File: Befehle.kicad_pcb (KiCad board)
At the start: 2 copper layers, 100 x 160 mm, 79 parts, among them J1 Conn_02x10_Odd_Even, J2 Conn_01x02, J3 Conn_01x04, J4 Conn_02x10_Odd_Even, J5 Conn_01x02, J6 Conn_01x03, U1 74LS14, U2 74LS541, U3 74LS540, U4 74LS139, U5 74LS373, U6 74540, U7 7402, U8 7408, U9 7400

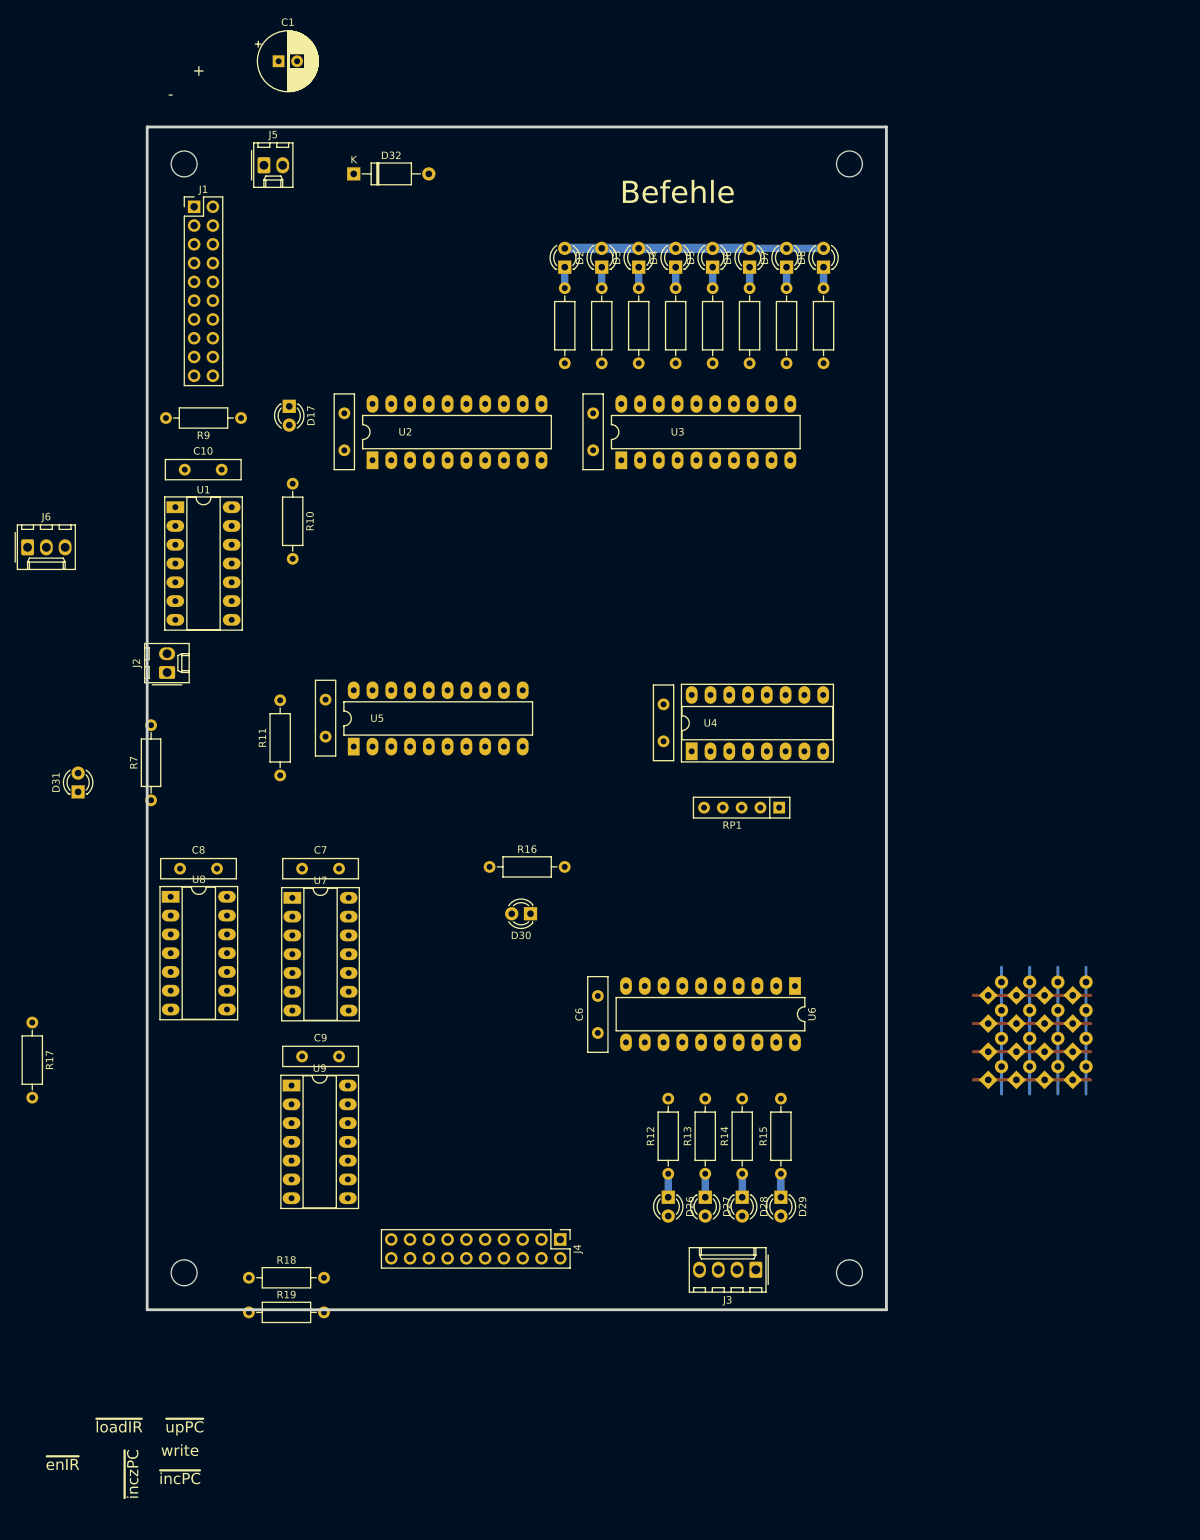
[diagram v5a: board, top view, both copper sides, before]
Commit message: Befehle: An der Platine weitergearbeitet
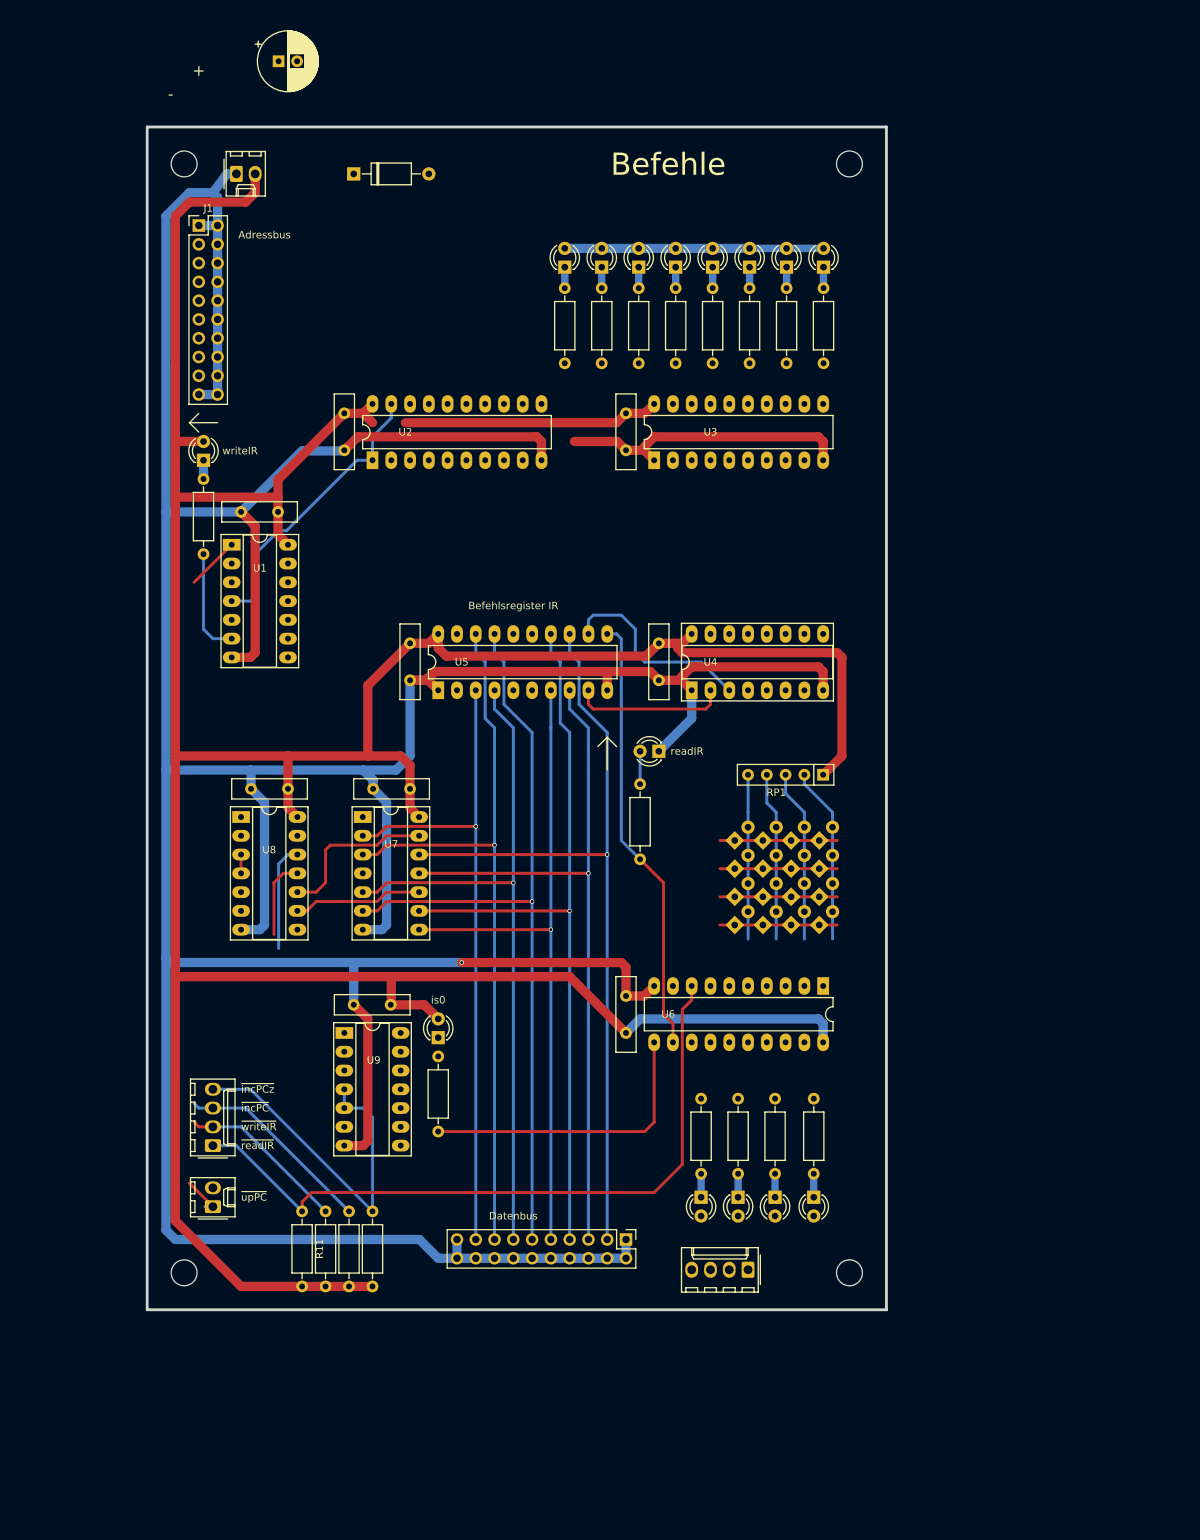
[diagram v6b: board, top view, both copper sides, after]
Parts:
- removed the R7 at (19.0, 111.1)
- J6: value Conn_01x03 -> Conn_01x04; footprint Connector_Molex:Molex_KK-254_AE-6410-03A_1x03_P2.54mm_Vertical -> Connector_Molex:Molex_KK-254_AE-6410-04A_1x04_P2.54mm_Vertical
- moved R9 118.0 mm to (42.6, 176.9), turned to 90 degrees
- moved J6 84.7 mm to (27.4, 157.8), turned to 90 degrees
- moved J2 72.5 mm to (27.4, 166.1)
- moved R11 59.0 mm to (39.5, 166.7), turned to 270 degrees
- moved D31 59.0 mm to (57.9, 143.2)
- moved R17 55.1 mm to (57.9, 145.8)
- moved D16 40.2 mm to (109.4, 120.4)
- moved D21 40.2 mm to (109.4, 124.2)
- moved D25 40.2 mm to (109.4, 128.0)
- moved D12 40.2 mm to (109.4, 116.6)
- moved D13 40.2 mm to (98.0, 120.4)
- moved D14 40.2 mm to (101.8, 120.4)
- moved D15 40.2 mm to (105.6, 120.4)
- moved D18 40.2 mm to (98.0, 124.2)
- moved D19 40.2 mm to (101.8, 124.2)
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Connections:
- J2 pad 1: loadIR -> ~upPC
- J2 pad 2: enableR -> Net-(J2-Pad2)
- J6 pad 1: upPC -> ~readIR
- J6 pad 2: incPCz -> ~writeIR
- J6 pad 3: incPC -> ~incPC
- R11 pad 1: loadIR -> ~readIR
- R9 pad 2: enableR -> ~writeIR
- U1 pad 1: enableR -> ~writeIR
- U5 pad 12: /a4 -> /b1
- U5 pad 13: /DB4 -> /DB7
- U5 pad 16: /b0 -> /a3
- U5 pad 17: /DB6 -> /DB3
- U5 pad 18: /DB7 -> /DB1
- U5 pad 19: /b1 -> /a1
- U5 pad 4: /DB1 -> /DB2
- U5 pad 5: /a1 -> /a2
- U5 pad 6: /a2 -> /a4
- U5 pad 7: /DB2 -> /DB4
- U5 pad 8: /DB3 -> /DB6
- U5 pad 9: /a3 -> /b0
- U6 pad 8: loadIR -> ~readIR
- U8 pad 14: Vcc -> VCC
- U8 pad 7: Gnd -> GND
- U9 pad 2: incPCz -> /incPCz
- U9 pad 6: incPCz -> /incPCz
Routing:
- net GND: track 0.00 -> 645.2 mm, vias 0 -> 1
- net VCC: track 35.1 -> 550.7 mm
- net /DB7: track 0.00 -> 109.5 mm, vias 0 -> 1
- net /DB3: track 0.00 -> 107.5 mm, vias 0 -> 1
- net /DB5: track 0.00 -> 103.3 mm, vias 0 -> 1
- net /DB1: track 0.00 -> 101.3 mm, vias 0 -> 1
- net /DB6: track 0.00 -> 98.3 mm, vias 0 -> 1
- net /DB2: track 0.00 -> 96.2 mm, vias 0 -> 1
- net ~readIR: track 0.00 -> 95.2 mm
- net /DB4: track 0.00 -> 92.1 mm, vias 0 -> 1
- net /DB0: track 0.00 -> 90.1 mm, vias 0 -> 1
- net Net-(R16-Pad2): track 0.00 -> 59.7 mm
- net ~incPCz: track 0.00 -> 48.0 mm
- net ~incPC: track 0.00 -> 41.5 mm
- net Net-(R17-Pad2): track 0.00 -> 40.5 mm
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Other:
- board text added: "Adressbus"
- board text added: "Befehlsregister IR"
- board text added: "Datenbus"
- board text added: "is0"
- board text added: "readIR"
- board text added: "writeIR"
- board text added: "~incPCz"
- board text added: "~readIR"
- board text added: "~writeIR"
- board text removed: "write"
- board text removed: "~enIR"
- board text removed: "~inczPC"
- board text removed: "~loadIR"

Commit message: Befehle: Platine fertig (TODO: Kontrolle)
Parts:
- U2, U3, U5, U6: footprint Package_DIP:DIP-20_W7.62mm_LongPads -> Package_DIP:DIP-20_W7.62mm_Socket_LongPads
- moved C1 16.1 mm to (41.4, 26.4), turned to 270 degrees
- moved C2 7.75 mm to (51.5, 63.2)
- moved U2 7.75 mm to (55.3, 69.6)
- moved R8 5.03 mm to (115.0, 51.8)
- moved D8 5.03 mm to (115.0, 39.1)
- moved R7 4.95 mm to (110.0, 51.8)
- moved D7 4.95 mm to (110.0, 39.1)
- moved R6 4.87 mm to (104.9, 51.8)
- moved D6 4.87 mm to (104.9, 39.1)
- moved R5 4.79 mm to (99.8, 51.8)
- moved D5 4.79 mm to (99.8, 39.1)
- moved R4 4.71 mm to (94.7, 51.8)
- moved D4 4.71 mm to (94.7, 39.1)
- moved R3 4.63 mm to (89.6, 51.8)
- moved D3 4.63 mm to (89.6, 39.1)
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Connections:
- U3 pad 2: /a7 -> /b1
- U3 pad 3: /a6 -> /b0
- U4 pad 10: (no net) -> Net-(U4-Pad10)
- U4 pad 11: (no net) -> Net-(U4-Pad11)
- U4 pad 12: (no net) -> Net-(U4-Pad12)
- U4 pad 13: (no net) -> VCC
- U4 pad 14: (no net) -> VCC
- U4 pad 15: (no net) -> VCC
- U4 pad 9: (no net) -> Net-(U4-Pad9)
- U6 pad 13: (no net) -> Net-(U6-Pad13)
- U6 pad 14: (no net) -> Net-(U6-Pad14)
- U6 pad 6: (no net) -> VCC
- U6 pad 7: (no net) -> VCC
- U9 pad 10: (no net) -> VCC
- U9 pad 11: (no net) -> Net-(U9-Pad11)
- U9 pad 12: (no net) -> VCC
- U9 pad 13: (no net) -> VCC
- U9 pad 14: Vcc -> VCC
- U9 pad 8: (no net) -> Net-(U9-Pad8)
- U9 pad 9: (no net) -> VCC
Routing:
- net VCC: track 550.7 -> 723.1 mm
- net /is0: track 0.00 -> 127.4 mm, vias 0 -> 1
- net /a0: track 0.00 -> 84.1 mm, vias 0 -> 1
- net ~writeIR: track 30.0 -> 110.6 mm
- net GND: track 645.2 -> 722.2 mm, vias 1 -> 3
- net /a2: track 0.00 -> 73.9 mm, vias 0 -> 1
- net /a1: track 0.00 -> 69.8 mm, vias 0 -> 1
- net /AB7: track 0.00 -> 68.0 mm
- net /AB6: track 0.00 -> 64.0 mm
- net /v0: track 23.8 -> 87.0 mm
- net /a4: track 0.00 -> 61.7 mm, vias 0 -> 1
- net /a3: track 0.00 -> 59.7 mm, vias 0 -> 1
- net /AB5: track 0.00 -> 59.7 mm
- net /v1: track 23.3 -> 80.5 mm
- net /AB4: track 0.00 -> 55.7 mm
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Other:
- board text added: "0"
- board text added: "1"
- board text added: "2"
- board text added: "3"
- board text added: "4"
- board text added: "5"
- board text added: "Adresse"
- board text added: "Befehl"
- board text added: "Befehlsdecoder"
- board text added: "Datenbus ist 0"
- board text added: "Mikroprogrammadresse"
- board text removed: "is0"

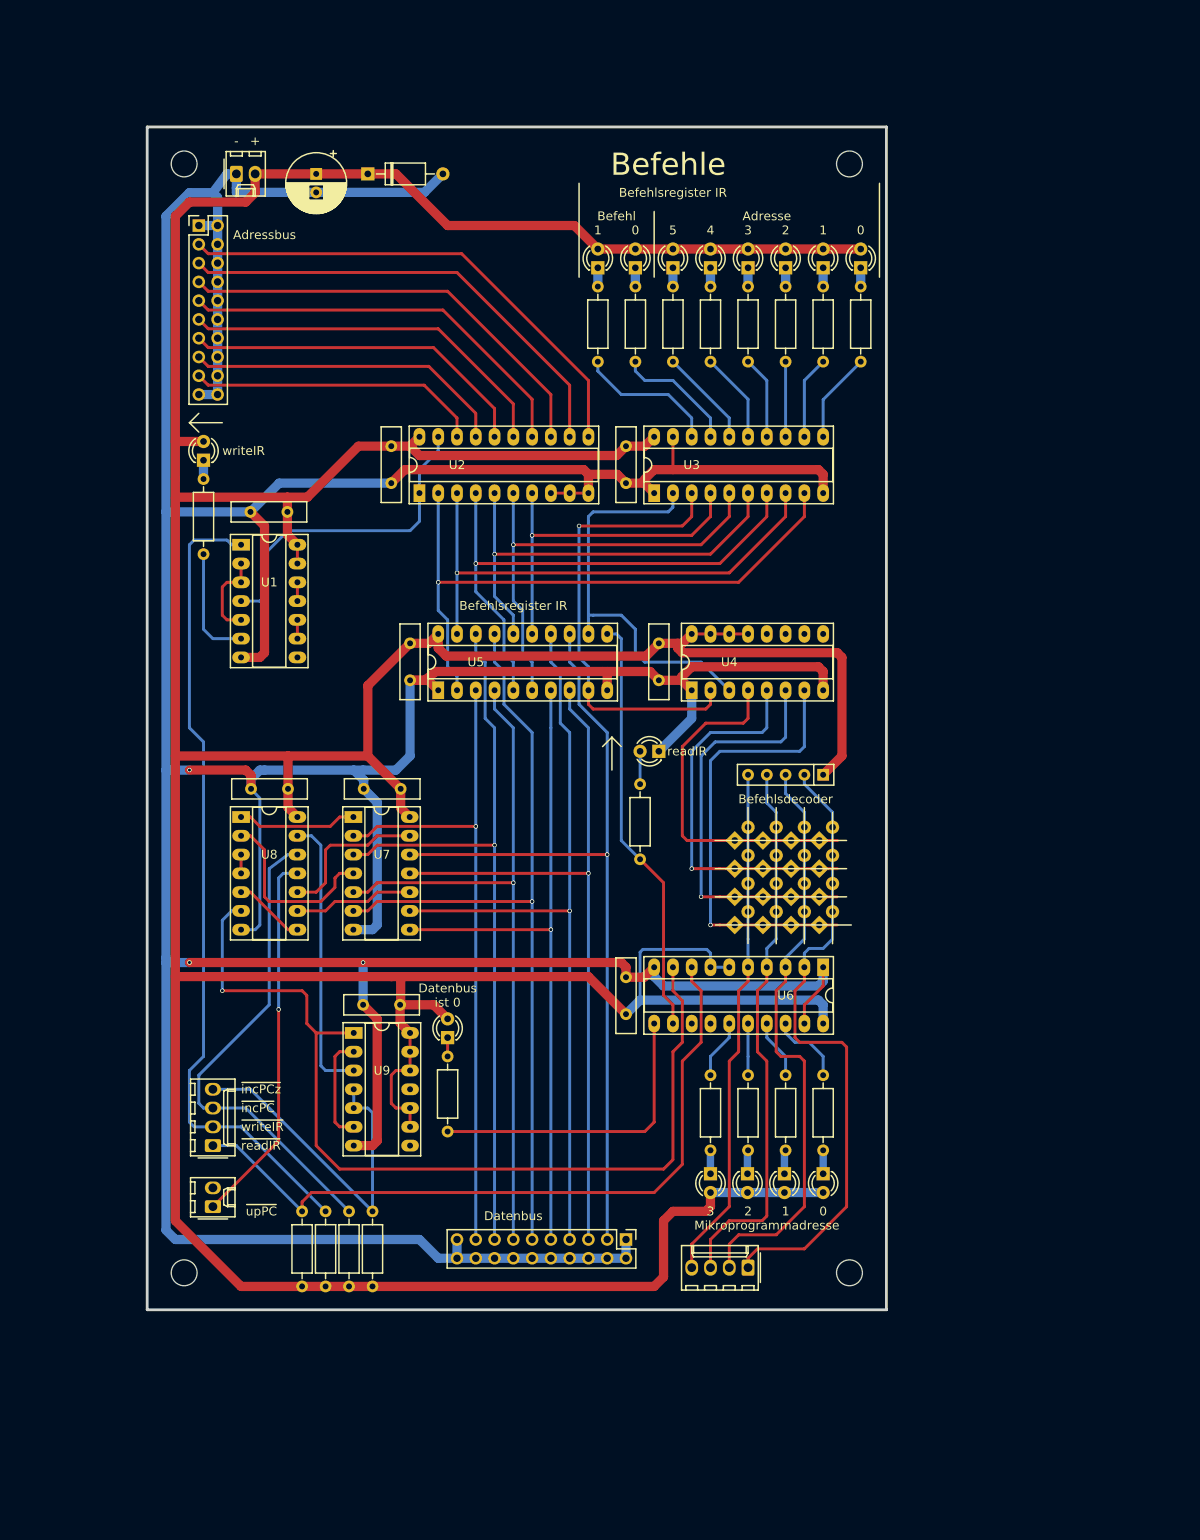
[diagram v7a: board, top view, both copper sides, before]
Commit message: Befehle und Steuerwerk: - Kleinkram - gerber rev 2.0 für Bestellung exportiert
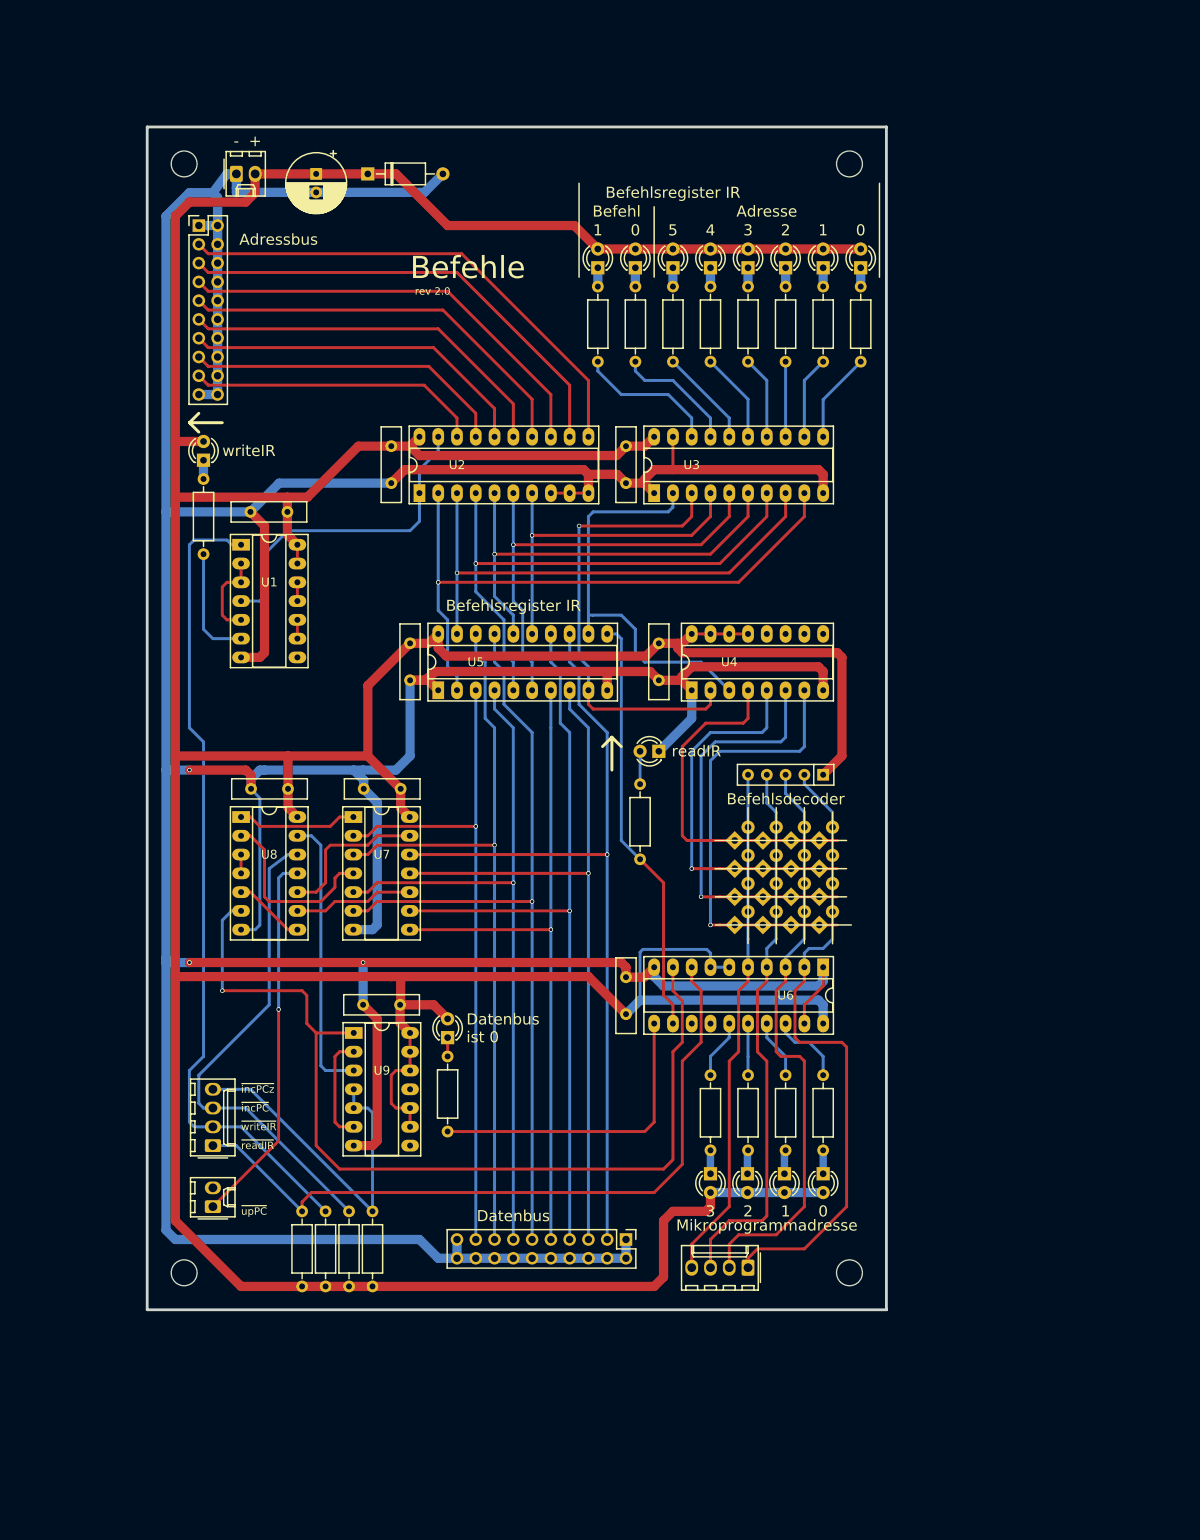
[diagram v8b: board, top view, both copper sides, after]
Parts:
- U4: value 74LS139 -> 74HC139
- U5: value 74LS373 -> 74HCT373
- U6: value 74540 -> 74HC540
- U7: value 7402 -> 74HCT02
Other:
- rule pad_to_mask_clearance: 0.2 -> 0.08
- rule solder_mask_min_width: 0.25 -> 0.254
- board text added: "rev 2.0"
